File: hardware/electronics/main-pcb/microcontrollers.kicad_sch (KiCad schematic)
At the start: 35 parts, among them IC8 ATSAME53J18A-MF, U6 ATSAMD11D14A-M, Y1 DSC6001CI2B-025.0000T

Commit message: worked on cmsis dap implementation aswell as cleaned up startup files for both microcontrolers
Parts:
- removed JP1, JP2: Jumper_2_Bridged, Jumper:SolderJumper-2_P1.3mm_Open_TrianglePad1.0x1.5mm, symbol Jumper:Jumper_2_Bridged
- added D36: CONNECT_LED, Diode_SMD:D_0603_1608Metric, symbol Device:LED
- added R63, R66: 1kΩ, Resistor_SMD:R_0603_1608Metric, symbol Device:R
- D35: value LED -> RUN_LED
- renumbered R63 to R64, R64 to R65
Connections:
- net +3.3V: now also R63.2
- net GND: now also D36.1 (K)
- net RESETN: now also U6.4 (PA05)
- net SERVO1_DB_CS: now also IC8.3 (PA02); no longer IC8.59 (PB30)
- net at IC8.58 (PA31): now also U6.7 (PA08), R63.1
- net at IC8.57 (PA30): now also U6.3 (PA04)
- net at U6.14 (PA17): now also R66.2
- net DBG_RESETN: now reaches R64.1, U6.18 (PA28/~{RESET})
- net at U6.6 (PA07): now also IC8.59 (PB30)
- new net: D36.2 (A), R66.1
- no-connect marks 29 -> 23
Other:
- note removed: "We need to interface with SWD in order to program the programmer initially"
- moved on the sheet: C82

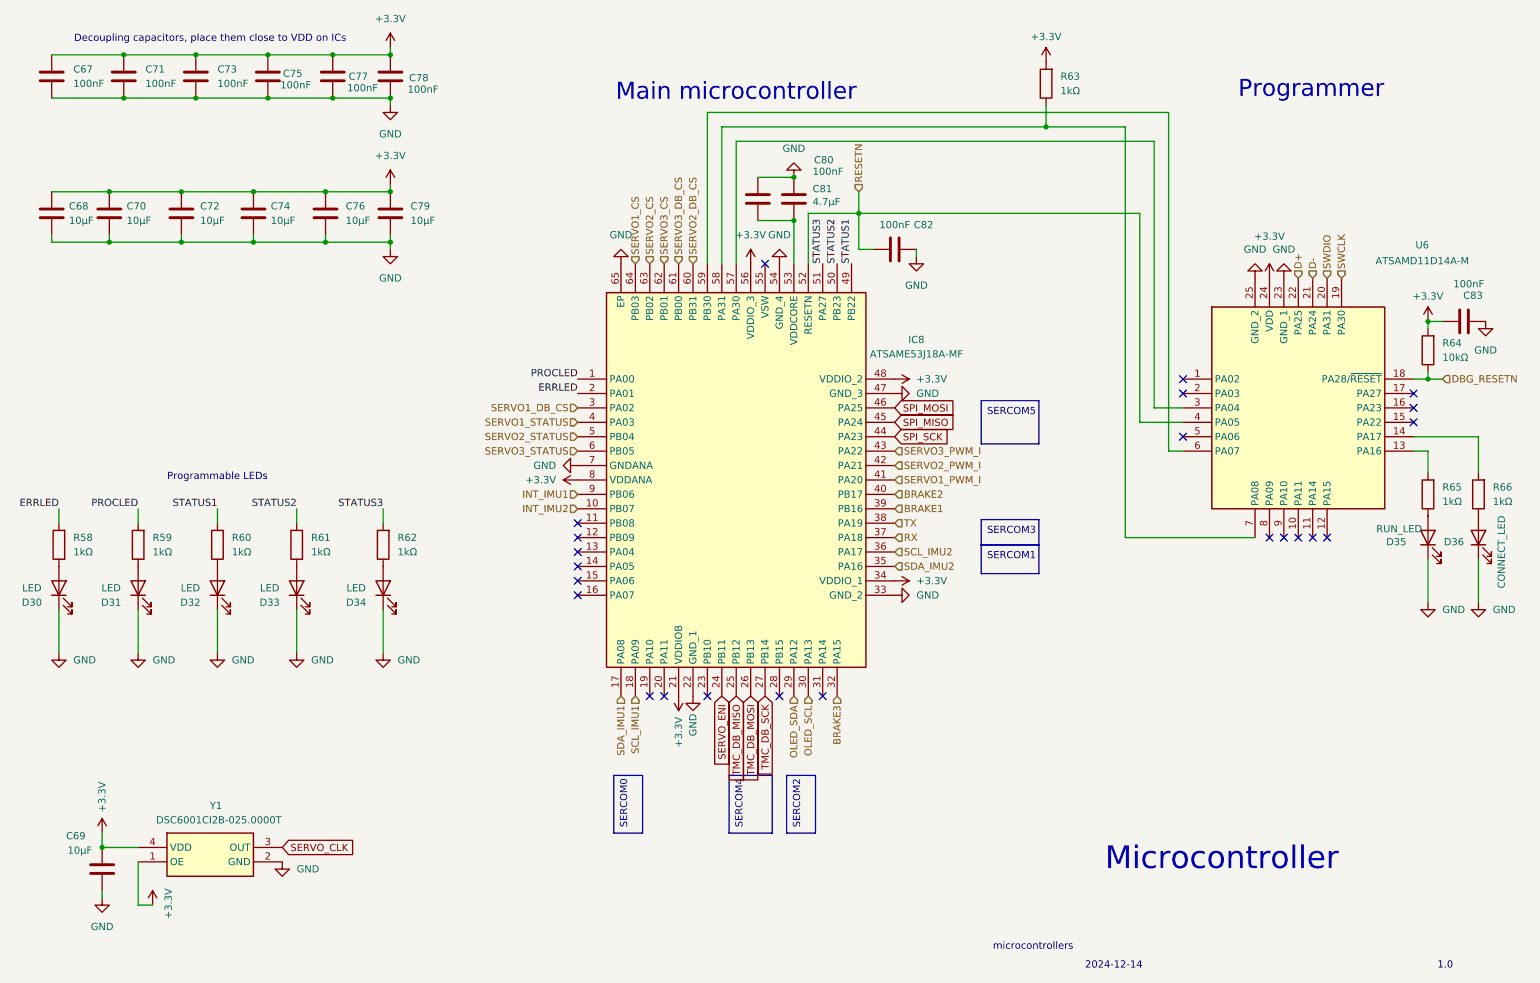
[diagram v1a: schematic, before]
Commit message: added new brake chopper logic, the previous was sketchy, still we might need to find better brake resistors than the one I added
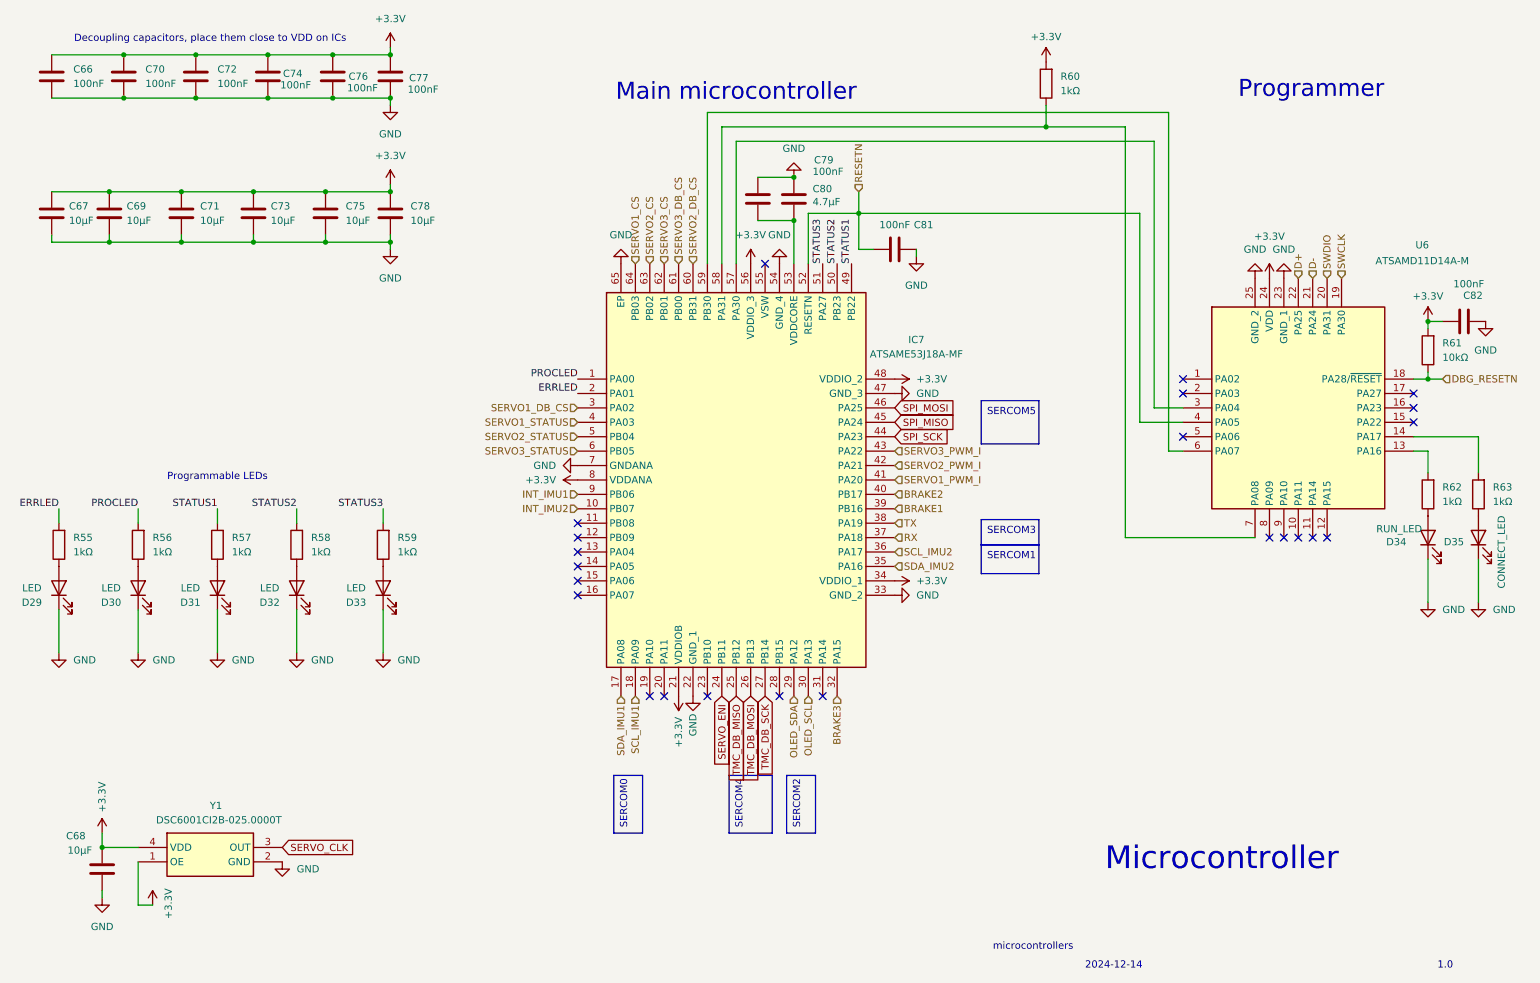
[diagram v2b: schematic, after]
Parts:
- renumbered C67 to C66, C68 to C67, C69 to C68, C70 to C69, C71 to C70, C72 to C71, C73 to C72, C74 to C73, C75 to C74, C76 to C75, C77 to C76, C78 to C77, C79 to C78, C80 to C79, C81 to C80, C82 to C81, C83 to C82, D30 to D29, D31 to D30, D32 to D31, D33 to D32, D34 to D33, D35 to D34, D36 to D35, IC8 to IC7, R58 to R55, R59 to R56, R60 to R57, R61 to R58, R62 to R59, R63 to R60, R64 to R61, R65 to R62, R66 to R63

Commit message: saved here
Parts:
- removed C68: 10µF, Capacitor_SMD:C_0603_1608Metric, symbol Device:C
- removed Y1: DSC6001CI2B-025.0000T, kuben-footprints:DSC6001CI2B0250000T, symbol DSC6001CI2B-025_0000T:DSC6001CI2B-025.0000T
- renumbered C66 to C67, C67 to C68
